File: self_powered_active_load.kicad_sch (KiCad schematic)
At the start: 90 parts, among them J1 Conn_01x05, J2 Conn_01x03, J3 BANANA_CONN, J4 BANANA_CONN, Q1 2SC4117, Q2 BDW94CFP, Q3 MMBT5401, Q5 MMBT5401, Q6 MMBT5401, U1 LM10CWM

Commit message: schematics documentation
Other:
- note added: "Decoupling for LM10"
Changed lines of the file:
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@@
+    (effects (font (size 1.27 1.27)) (justify left bottom))
+  )
+  (text "Decoupling\nfor LM10" (at 106.934 34.544 0)
     (effects (font (size 1.27 1.27)) (justify left bottom))
   )

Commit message: schematics documentation
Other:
- note added: "four Sziklai output stages"
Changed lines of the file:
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@@
     )
+  )
+  (text "four Sziklai output stages" (at 208.28 46.99 0)
+    (effects (font (size 1.27 1.27)) (justify left bottom))
   )
   (text "Switch" (at 26.67 179.705 0)

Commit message: schematics documentation
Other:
- note added: "Fischer LA6 150mm"
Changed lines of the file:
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@@
+    (effects (font (size 1.27 1.27)) (justify left bottom))
+  )
+  (text "Fischer LA6 150mm" (at 140.716 61.468 0)
     (effects (font (size 1.27 1.27)) (justify left bottom))
   )

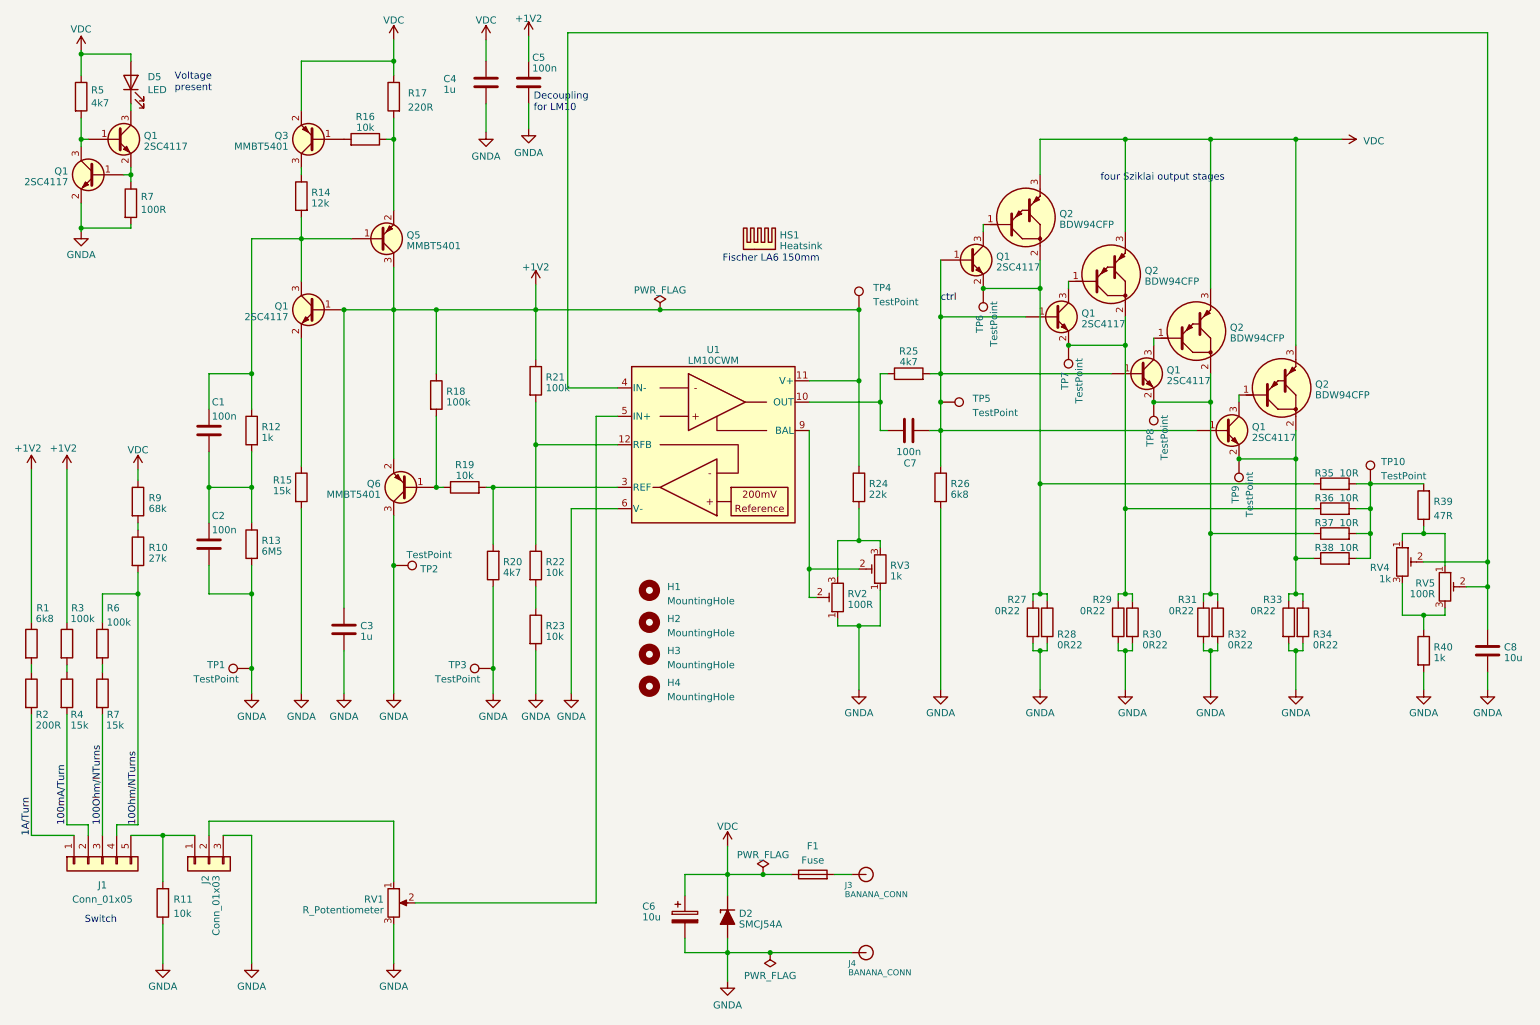
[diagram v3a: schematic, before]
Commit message: Name added on PCB
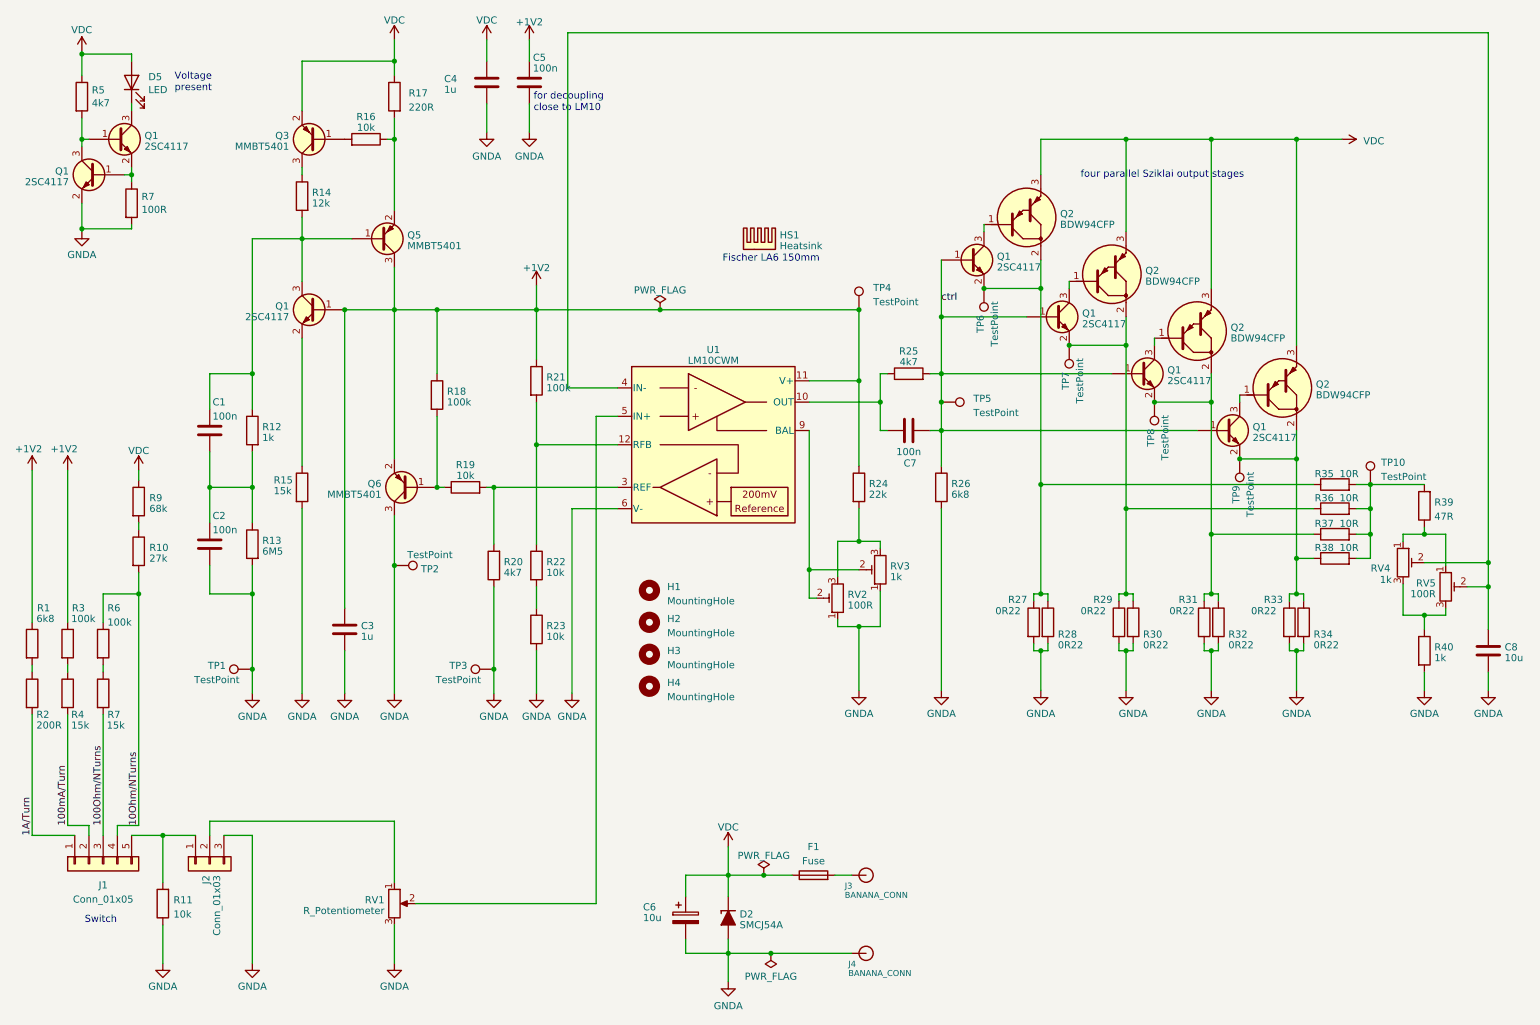
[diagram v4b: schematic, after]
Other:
- note added: "for decoupling close to LM10"
- note added: "four parallel Sziklai output stages"
- note removed: "Decoupling for LM10"
- note removed: "four Sziklai output stages"
